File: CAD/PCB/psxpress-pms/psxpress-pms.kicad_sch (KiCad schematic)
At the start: 40 parts, among them IC1 BQ25606RGER, IC2 MAX16054AZT+T, IC3 TPS61023DRLT, IC4 TPS564255DRLR, Q1 AONR21117, SW1 SW_SPST

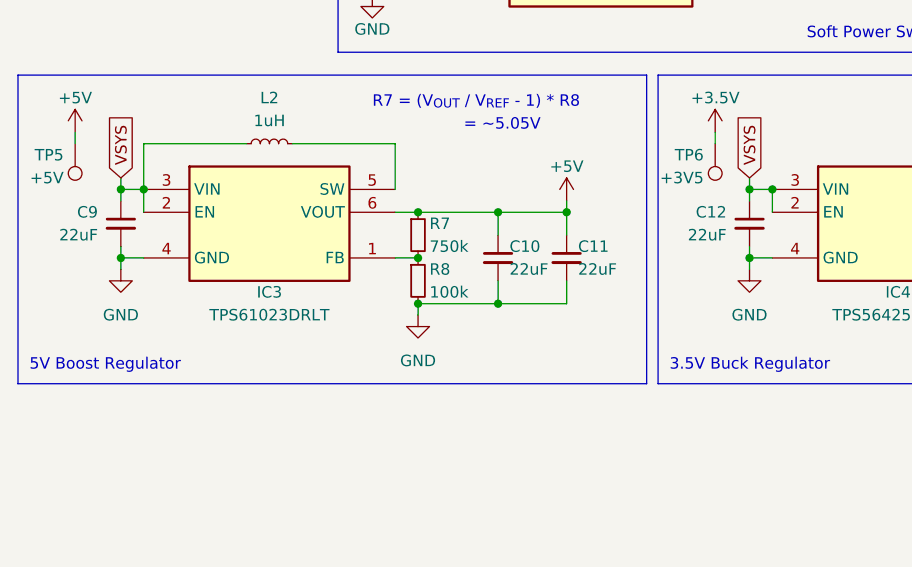
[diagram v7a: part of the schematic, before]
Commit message: pms - add voltage reg solder pads + preliminary board edge cuts
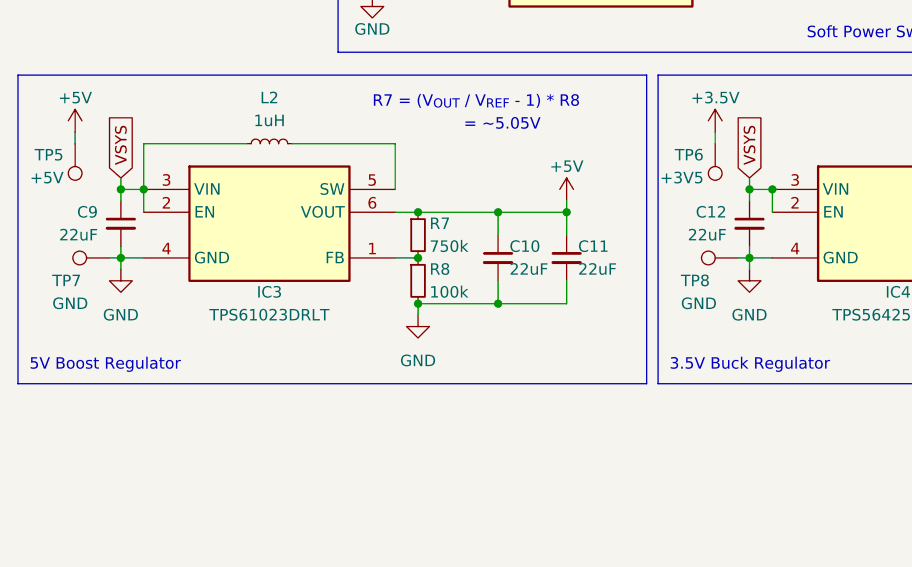
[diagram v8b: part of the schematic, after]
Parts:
- added TP7, TP8: GND, solderpads:power_pad_2.5x1.5mm, symbol Connector:TestPoint
- TP1, TP3, TP5, TP6: footprint (none) -> solderpads:power_pad_2.5x1.5mm
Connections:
- net GND: now also TP7.1, TP8.1
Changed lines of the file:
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@@
+    (stroke (width 0) (type default))
+  )
+  (wire (pts (xy 157.48 140.97) (xy 158.75 140.97))
     (stroke (width 0) (type default))
   )
@@
   )
   (wire (pts (xy 134.62 66.04) (xy 140.97 66.04))
+    (stroke (width 0) (type default))
+  )
+  (wire (pts (xy 87.63 140.97) (xy 88.9 140.97))
     (stroke (width 0) (type default))
   )
@@
       (effects (font (size 1.27 1.27)) (justify left))
     )
-    (property "Footprint" "" (at 78.74 128.27 0)
+    (property "Footprint" "solderpads:power_pad_2.5x1.5mm" (at 78.74 128.27 0)
       (effects (font (size 1.27 1.27)) hide)
     )
@@
     )
   )
+  (symbol (lib_id "Connector:TestPoint") (at 87.63 140.97 90) (unit 1)
+    (in_bom yes) (on_board yes) (dnp no)
+    (property "Reference" "TP7" (at 81.28 143.51 90)
+      (effects (font (size 1.27 1.27)) (justify right))
+    )
+    (property "Value" "GND" (at 81.28 146.05 90)
+      (effects (font (size 1.27 1.27)) (justify right))
+    )
+    (property "Footprint" "solderpads:power_pad_2.5x1.5mm" (at 87.63 135.89 0)
+      (effects (font (size 1.27 1.27)) hide)
+    )
+    (property "Datasheet" "~" (at 87.63 135.89 0)
+      (effects (font (size 1.27 1.27)) hide)
+    )
+    (pin "1")
+    (instances
+      (project "psxpress-pms"
+        (path "/b46ebcbe-5ef3-41ff-bf92-95c75415e5a2"
+          (reference "TP7") (unit 1)
+        )
+      )
+    )
+  )
   (symbol (lib_id "power:+5V") (at 102.87 102.87 0) (unit 1)
     (in_bom yes) (on_board yes) (dnp no)
@@
       (effects (font (size 1.27 1.27)) (justify right))
     )
-    (property "Footprint" "" (at 134.62 53.34 0)
+    (property "Footprint" "solderpads:power_pad_2.5x1.5mm" (at 134.62 53.34 0)
       (effects (font (size 1.27 1.27)) hide)
     )
@@
       (effects (font (size 1.27 1.27)) (justify right))
     )
-    (property "Footprint" "" (at 97.79 80.01 0)
+    (property "Footprint" "solderpads:power_pad_2.5x1.5mm" (at 97.79 80.01 0)
       (effects (font (size 1.27 1.27)) hide)
     )
@@
         (path "/b46ebcbe-5ef3-41ff-bf92-95c75415e5a2"
           (reference "TP1") (unit 1)
+        )
+      )
+    )
+  )
+  (symbol (lib_id "Connector:TestPoint") (at 157.48 140.97 90) (unit 1)
+    (in_bom yes) (on_board yes) (dnp no)
+    (property "Reference" "TP8" (at 151.13 143.51 90)
+      (effects (font (size 1.27 1.27)) (justify right))
+    )
+    (property "Value" "GND" (at 151.13 146.05 90)
+      (effects (font (size 1.27 1.27)) (justify right))
+    )
+    (property "Footprint" "solderpads:power_pad_2.5x1.5mm" (at 157.48 135.89 0)
+      (effects (font (size 1.27 1.27)) hide)
+    )
+    (property "Datasheet" "~" (at 157.48 135.89 0)
+      (effects (font (size 1.27 1.27)) hide)
+    )
+    (pin "1")
+    (instances
+      (project "psxpress-pms"
+        (path "/b46ebcbe-5ef3-41ff-bf92-95c75415e5a2"
+          (reference "TP8") (unit 1)
         )
       )
@@
       (effects (font (size 1.27 1.27)) (justify left))
     )
-    (property "Footprint" "" (at 149.86 128.27 0)
-      (effects (font (size 1.27 1.27)) hide)
-    )
+    (property "Footprint" "solderpads:power_pad_2.5x1.5mm" (at 149.86 128.27 0)
+      (effects (font (size 1.27 1.27)) hide)
+    )
